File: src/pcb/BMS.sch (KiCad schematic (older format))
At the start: 0 parts

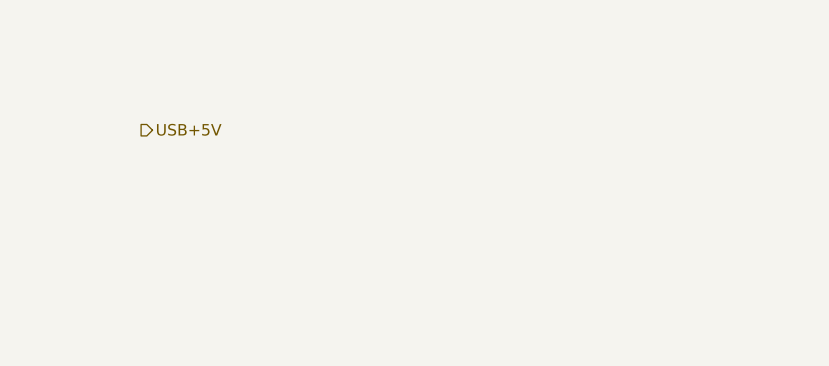
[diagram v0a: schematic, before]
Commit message: added more connections, clarified schematic. Also added missing schematics
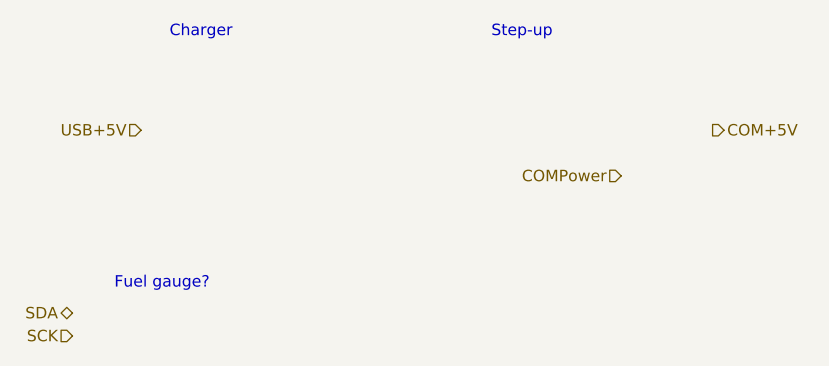
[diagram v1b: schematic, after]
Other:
- note added: "Charger"
- note added: "Fuel gauge?"
- note added: "Step-up"
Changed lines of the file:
@@
 Comment4 ""
 $EndDescr
-Text HLabel 4100 2900 2    50   Output ~ 0
+Text HLabel 4100 2900 0    50   Input ~ 0
 USB+5V
+Text HLabel 6600 2900 2    50   Output ~ 0
+COM+5V
+Text HLabel 6200 3100 0    50   Input ~ 0
+COMPower
+Text HLabel 3800 3700 0    50   BiDi ~ 0
+SDA
+Text HLabel 3800 3800 0    50   Input ~ 0
+SCK
+Text Notes 4400 3600 2    50   ~ 0
+Fuel gauge?
+Text Notes 4500 2500 2    50   ~ 0
+Charger
+Text Notes 5900 2500 2    50   ~ 0
+Step-up
 $EndSCHEMATC
